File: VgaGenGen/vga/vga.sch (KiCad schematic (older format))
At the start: 22 parts, among them X25.175MHz CXO_DIP14

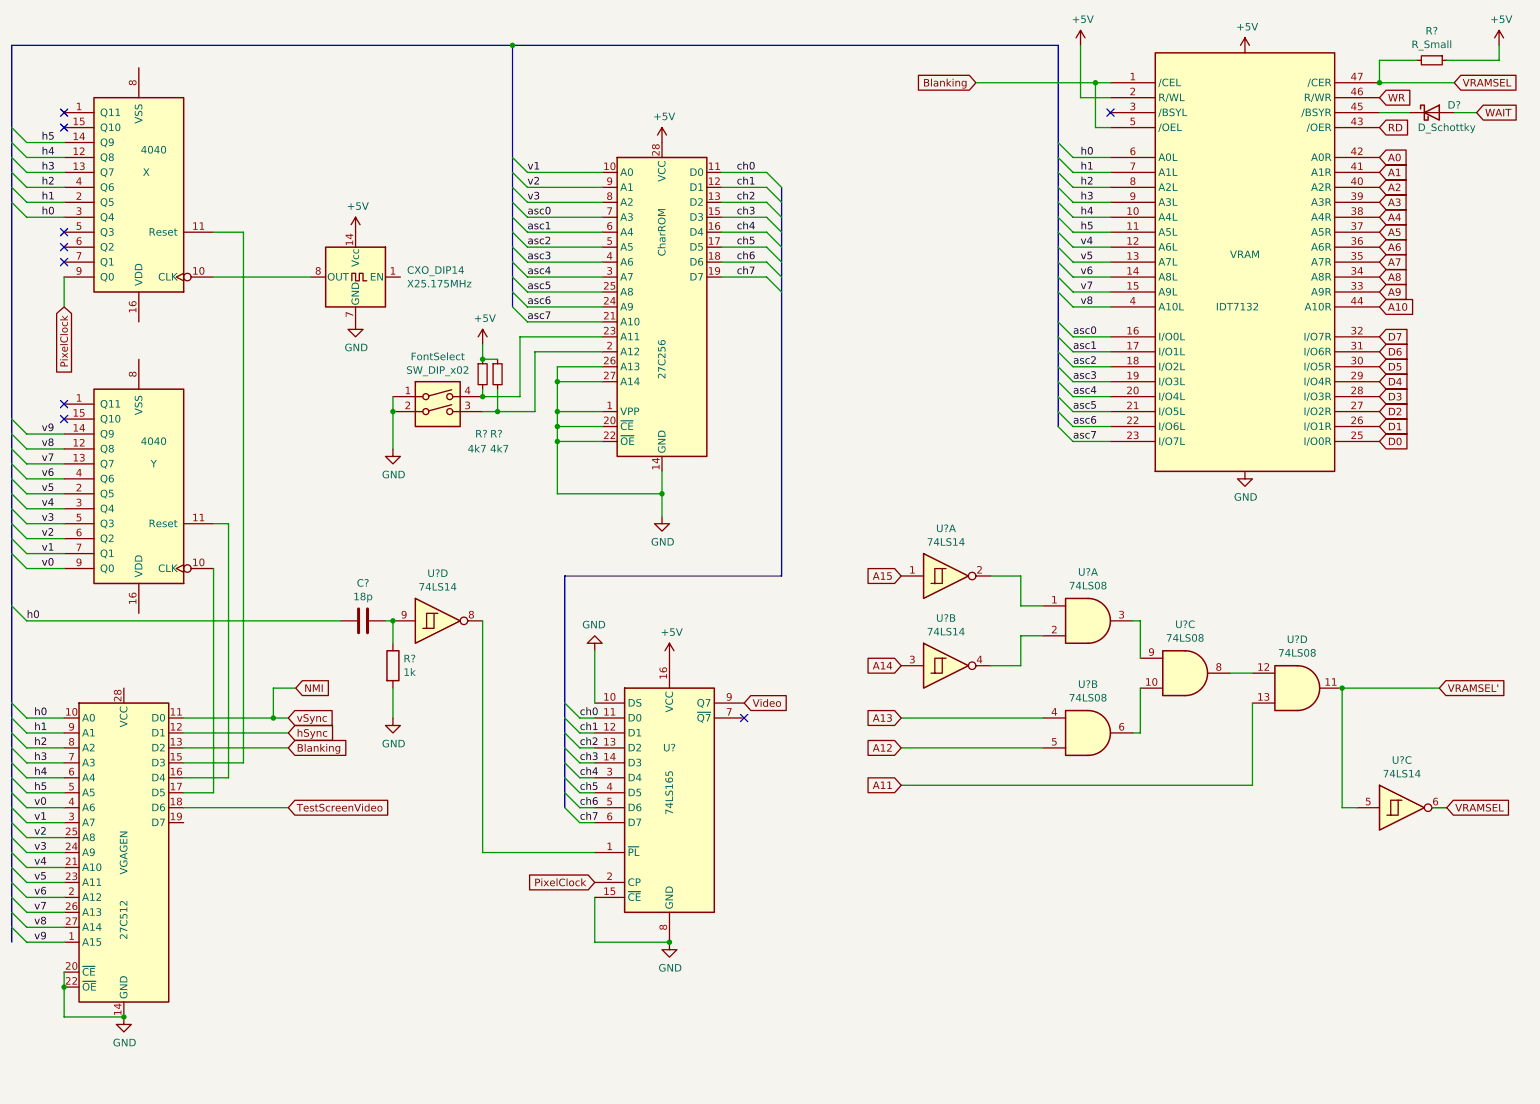
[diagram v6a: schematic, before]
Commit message: corrections to the VGA schematic, added vga.asm
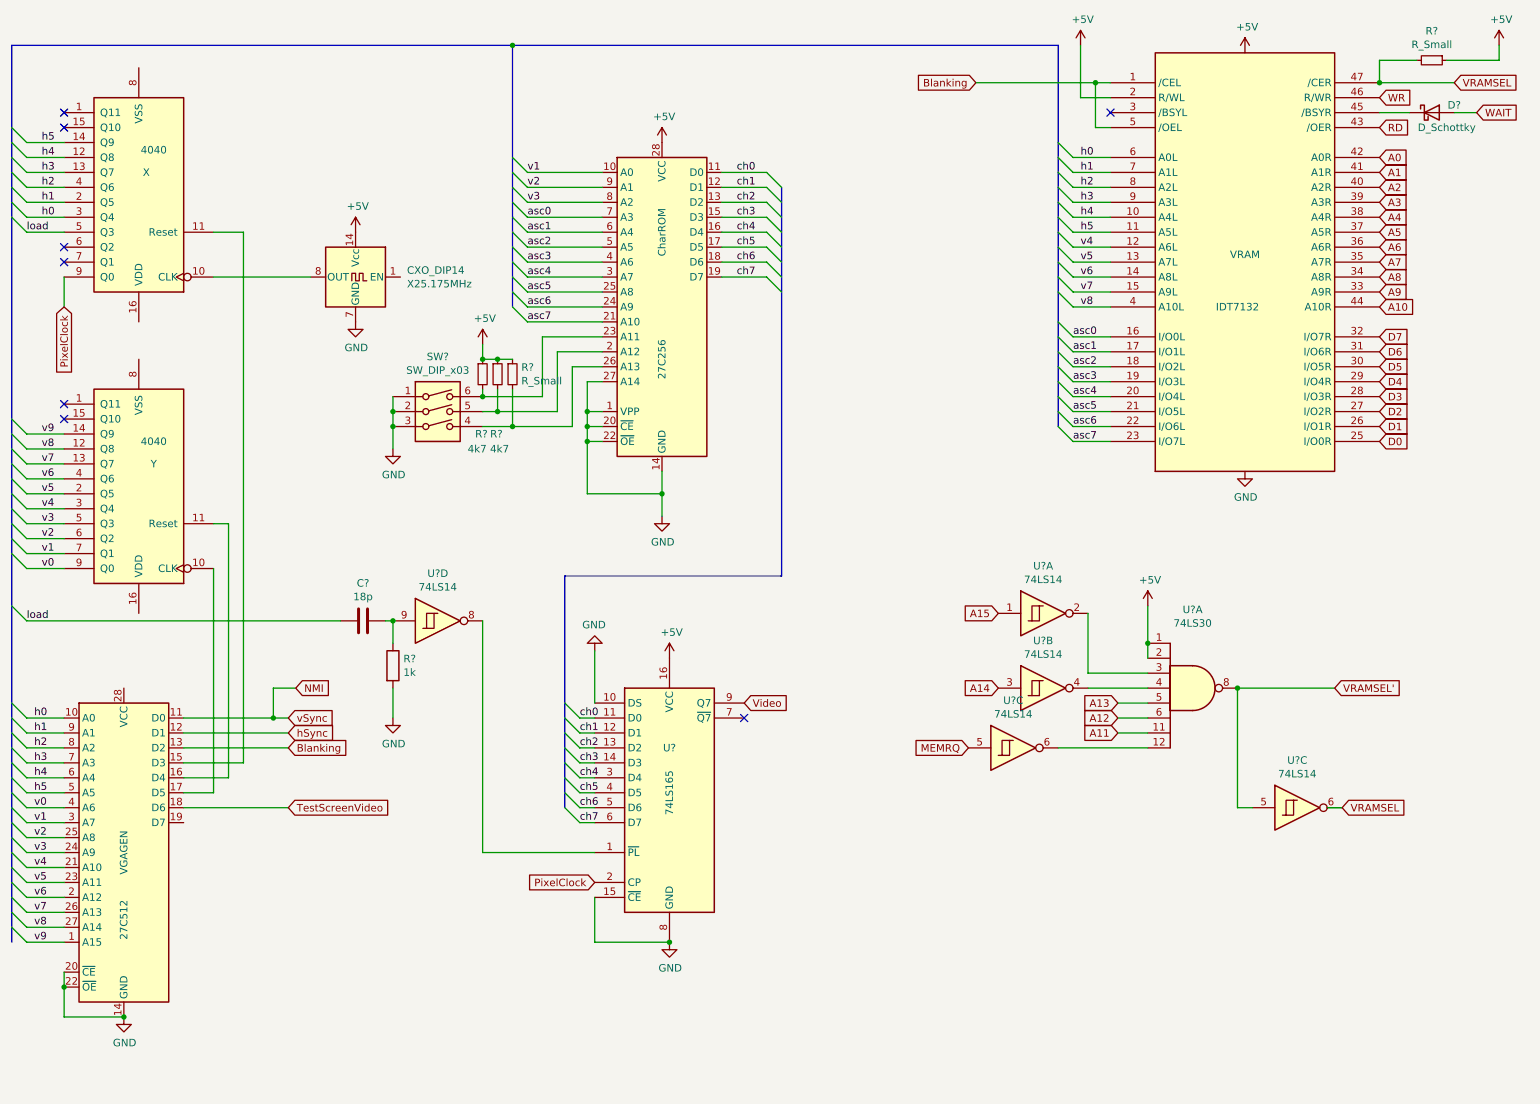
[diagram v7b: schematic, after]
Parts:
- removed FontSelect: SW_DIP_x02, symbol Switch:SW_DIP_x02
- removed U? (x4): 74LS08, symbol 74xx:74LS08
- added R?: R_Small, symbol Device:R_Small
- added SW?: SW_DIP_x03, symbol Switch:SW_DIP_x03
- added U?: 74LS30, symbol 74xx:74LS30
- added U?: 74LS14, symbol 74xx:74LS14
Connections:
- net +5V: now also R?.1, U?.1, U?.2
- net A11: now also U?.11
- net A12: now also U?.6
- net A13: now also U?.5
- net GND: now also SW?.1, SW?.2, SW?.3; no longer CharROM.26 (A13)
- net VRAMSEL': now also U?.8
- net h0: no longer C?.1
- net load: now reaches X.5 (Q3)
- net load: now also C?.1
- net at U?.2: now also U?.3
- net at U?.4: now also U?.4
- net at CharROM.2 (A12), R?.2: now also SW?.5
- net at CharROM.23 (A11), R?.2: now also SW?.6
- new net: CharROM.26 (A13), R?.2, SW?.4
- new net: U?.12, U?.6
- new net MEMRQ: U?.5
- no-connect marks 9 -> 8
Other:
- moved on the sheet: U?A, U?B, U?C
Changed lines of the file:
@@
 Entry Wire Line
 	950  4450 1050 4550
-Text Label 1050 4550 0    50   ~ 0
-h0
 Text GLabel 5850 5100 2    50   Input ~ 0
 Video
@@
 	1    0    0    -1
 $EndComp
-NoConn ~ 1300 1950
 NoConn ~ 1300 2050
 NoConn ~ 1300 2150
@@
 Wire Wire Line
 	8100 1050 8300 1050
-$Comp
-L Memory_EPROM:27C256 CharROM
-U 1 1 62173F7D
-P 5300 2450
-F 0 "CharROM" V 5300 2950 50  0000 C CNN
-F 1 "27C256" V 5300 2100 50  0000 C CNN
-F 2 "Package_DIP:DIP-28_W15.24mm" H 5300 2450 50  0001 C CNN
-F 3 "http://ww1.microchip.com/downloads/en/DeviceDoc/doc0014.pdf" H 5300 2450 50  0001 C CNN
-	1    5300 2450
-	1    0    0    -1
-$EndComp
 Entry Wire Line
 	6100 1650 6000 1550
@@
 	4900 2550 4400 2550
 Wire Wire Line
-	4600 3700 5300 3700
-Wire Wire Line
 	5300 3550 5300 3700
 Connection ~ 5300 3700
@@
 	5300 3700 5300 3850
 Wire Wire Line
-	4900 2850 4600 2850
-Wire Wire Line
-	4600 2850 4600 2950
-Wire Wire Line
-	4900 2950 4600 2950
-Connection ~ 4600 2950
-Wire Wire Line
-	4600 2950 4600 3150
-Wire Wire Line
-	4900 3150 4600 3150
-Connection ~ 4600 3150
-Wire Wire Line
-	4600 3150 4600 3250
-Wire Wire Line
-	4900 3250 4600 3250
-Connection ~ 4600 3250
-Wire Wire Line
-	4600 3250 4600 3350
-Wire Wire Line
-	4900 3350 4600 3350
-Connection ~ 4600 3350
-Wire Wire Line
-	4600 3350 4600 3700
+	4900 2950 4800 2950
 $Comp
 L power:+5V #PWR?
@@
 L 74xx:74LS14 U?
 U 1 1 6216906C
-P 7200 4250
-F 0 "U?" H 7200 4567 50  0000 C CNN
-F 1 "74LS14" H 7200 4476 50  0000 C CNN
-F 2 "" H 7200 4250 50  0001 C CNN
-F 3 "http://www.ti.com/lit/gpn/sn74LS14" H 7200 4250 50  0001 C CNN
-	1    7200 4250
+P 7850 4500
+F 0 "U?" H 7850 4817 50  0000 C CNN
+F 1 "74LS14" H 7850 4726 50  0000 C CNN
+F 2 "" H 7850 4500 50  0001 C CNN
+F 3 "http://www.ti.com/lit/gpn/sn74LS14" H 7850 4500 50  0001 C CNN
+	1    7850 4500
 	1    0    0    -1
 $EndComp
@@
 L 74xx:74LS14 U?
 U 2 1 62169072
-P 7200 4850
-F 0 "U?" H 7200 5167 50  0000 C CNN
-F 1 "74LS14" H 7200 5076 50  0000 C CNN
-F 2 "" H 7200 4850 50  0001 C CNN
-F 3 "http://www.ti.com/lit/gpn/sn74LS14" H 7200 4850 50  0001 C CNN
-	2    7200 4850
+P 7850 5000
+F 0 "U?" H 7850 5317 50  0000 C CNN
+F 1 "74LS14" H 7850 5226 50  0000 C CNN
+F 2 "" H 7850 5000 50  0001 C CNN
+F 3 "http://www.ti.com/lit/gpn/sn74LS14" H 7850 5000 50  0001 C CNN
+	2    7850 5000
 	1    0    0    -1
 $EndComp
@@
 L 74xx:74LS14 U?
 U 3 1 62169078
-P 10250 5800
-F 0 "U?" H 10250 6117 50  0000 C CNN
-F 1 "74LS14" H 10250 6026 50  0000 C CNN
-F 2 "" H 10250 5800 50  0001 C CNN
-F 3 "http://www.ti.com/lit/gpn/sn74LS14" H 10250 5800 50  0001 C CNN
-	3    10250 5800
-	1    0    0    -1
-$EndComp
-$Comp
-L 74xx:74LS08 U?
-U 1 1 6216907E
-P 8150 4550
-F 0 "U?" H 8150 4875 50  0000 C CNN
-F 1 "74LS08" H 8150 4784 50  0000 C CNN
-F 2 "" H 8150 4550 50  0001 C CNN
-F 3 "http://www.ti.com/lit/gpn/sn74LS08" H 8150 4550 50  0001 C CNN
-	1    8150 4550
-	1    0    0    -1
-$EndComp
-$Comp
-L 74xx:74LS08 U?
-U 2 1 62169084
-P 8150 5300
-F 0 "U?" H 8150 5625 50  0000 C CNN
-F 1 "74LS08" H 8150 5534 50  0000 C CNN
-F 2 "" H 8150 5300 50  0001 C CNN
-F 3 "http://www.ti.com/lit/gpn/sn74LS08" H 8150 5300 50  0001 C CNN
-	2    8150 5300
-	1    0    0    -1
-$EndComp
-$Comp
-L 74xx:74LS08 U?
-U 3 1 6216908A
-P 8800 4900
-F 0 "U?" H 8800 5225 50  0000 C CNN
-F 1 "74LS08" H 8800 5134 50  0000 C CNN
-F 2 "" H 8800 4900 50  0001 C CNN
-F 3 "http://www.ti.com/lit/gpn/sn74LS08" H 8800 4900 50  0001 C CNN
-	3    8800 4900
-	1    0    0    -1
-$EndComp
-$Comp
-L 74xx:74LS08 U?
-U 4 1 62169090
-P 9550 5000
-F 0 "U?" H 9550 5325 50  0000 C CNN
-F 1 "74LS08" H 9550 5234 50  0000 C CNN
-F 2 "" H 9550 5000 50  0001 C CNN
-F 3 "http://www.ti.com/lit/gpn/sn74LS08" H 9550 5000 50  0001 C CNN
-	4    9550 5000
-	1    0    0    -1
-$EndComp
-Wire Wire Line
-	8500 4800 8500 4550
-Wire Wire Line
-	8500 4550 8450 4550
-Wire Wire Line
-	8500 5000 8500 5300
-Wire Wire Line
-	8500 5300 8450 5300
-Wire Wire Line
-	7850 4450 7700 4450
-Wire Wire Line
-	7700 4450 7700 4250
-Wire Wire Line
-	7700 4250 7500 4250
-Wire Wire Line
-	7500 4850 7700 4850
-Wire Wire Line
-	7700 4850 7700 4650
-Wire Wire Line
-	7700 4650 7850 4650
-Wire Wire Line
-	9850 5000 9850 5800
-Wire Wire Line
-	9850 5800 9950 5800
-Wire Wire Line
-	9100 4900 9250 4900
-Text GLabel 10550 5800 2    50   Input ~ 0
+P 9550 5800
+F 0 "U?" H 9550 6117 50  0000 C CNN
+F 1 "74LS14" H 9550 6026 50  0000 C CNN
+F 2 "" H 9550 5800 50  0001 C CNN
+F 3 "http://www.ti.com/lit/gpn/sn74LS14" H 9550 5800 50  0001 C CNN
+	3    9550 5800
+	1    0    0    -1
+$EndComp
+Wire Wire Line
+	9150 5000 9150 5800
+Wire Wire Line
+	9150 5800 9250 5800
+Text GLabel 9850 5800 2    50   Input ~ 0
 VRAMSEL
-Text GLabel 10500 5000 2    50   Input ~ 0
+Text GLabel 9800 5000 2    50   Input ~ 0
 VRAMSEL'
-Connection ~ 9850 5000
-Text GLabel 6900 4850 0    50   Input ~ 0
+Text GLabel 7550 5000 0    50   Input ~ 0
 A14
-Text GLabel 6900 4250 0    50   Input ~ 0
+Text GLabel 7550 4500 0    50   Input ~ 0
 A15
-Text GLabel 6900 5200 0    50   Input ~ 0
+Text GLabel 8350 5100 0    50   Input ~ 0
 A13
-Text GLabel 6900 5400 0    50   Input ~ 0
+Text GLabel 8350 5200 0    50   Input ~ 0
 A12
-Text GLabel 6900 5650 0    50   Input ~ 0
+Text GLabel 8350 5300 0    50   Input ~ 0
 A11
 Wire Wire Line
-	6900 5200 7850 5200
-Wire Wire Line
-	7850 5400 6900 5400
-Wire Wire Line
-	6900 5650 9250 5650
-Wire Wire Line
-	9250 5100 9250 5650
-Wire Wire Line
-	10450 5800 10550 5800
-Wire Wire Line
-	10500 5000 9850 5000
+	9750 5800 9850 5800
+Wire Wire Line
+	9800 5000 9150 5000
 Wire Bus Line
 	950  700  4300 700
@@
 Wire Bus Line
 	4300 700  7950 700
-$Comp
-L Switch:SW_DIP_x02 FontSelect
-U 1 1 621A6CFD
-P 3800 3150
-F 0 "FontSelect" H 3800 3517 50  0000 C CNN
-F 1 "SW_DIP_x02" H 3800 3426 50  0000 C CNN
-F 2 "" H 3800 3150 50  0001 C CNN
-F 3 "~" H 3800 3150 50  0001 C CNN
-	1    3800 3150
-	1    0    0    -1
-$EndComp
 $Comp
 L power:GND #PWR?
@@
 $EndComp
 Wire Wire Line
-	3500 3400 3500 3150
-Connection ~ 3500 3150
-Wire Wire Line
-	3500 3150 3500 3050
-Wire Wire Line
-	4900 2750 4450 2750
-Wire Wire Line
-	4450 2750 4450 3150
-Wire Wire Line
-	4450 3150 4200 3150
-Wire Wire Line
-	4900 2650 4350 2650
-Wire Wire Line
-	4350 2650 4350 3050
-Wire Wire Line
-	4350 3050 4100 3050
+	4900 2750 4600 2750
+Wire Wire Line
+	4900 2650 4500 2650
 $Comp
 L Device:R_Small R?
@@
 Wire Wire Line
 	4100 3000 4100 3050
-Connection ~ 4100 3050
 Wire Wire Line
 	4200 2800 4100 2800
@@
 Wire Wire Line
 	10900 800  10900 700
+$Comp
+L 74xx:74LS30 U?
+U 1 1 623C44D8
+P 8850 5000
+F 0 "U?" H 8850 5525 50  0000 C CNN
+F 1 "74LS30" H 8850 5434 50  0000 C CNN
+F 2 "" H 8850 5000 50  0001 C CNN
+F 3 "http://www.ti.com/lit/gpn/sn74LS30" H 8850 5000 50  0001 C CNN
+	1    8850 5000
+	1    0    0    -1
+$EndComp
+Wire Wire Line
+	8350 5100 8550 5100
+Wire Wire Line
+	8350 5200 8550 5200
+Wire Wire Line
+	8350 5300 8550 5300
+Wire Wire Line
+	8550 5000 8150 5000
+Wire Wire Line
+	8550 4900 8150 4900
+Wire Wire Line
+	8150 4900 8150 4500
+$Comp
+L power:+5V #PWR?
+U 1 1 62458EBA
+P 8550 4450
+F 0 "#PWR?" H 8550 4300 50  0001 C CNN
+F 1 "+5V" H 8565 4623 50  0000 C CNN
+F 2 "" H 8550 4450 50  0001 C CNN
+F 3 "" H 8550 4450 50  0001 C CNN
+	1    8550 4450
+	1    0    0    -1
+$EndComp
+Wire Wire Line
+	8550 4450 8550 4700
+Connection ~ 8550 4700
+Wire Wire Line
+	8550 4700 8550 4800
+Connection ~ 9150 5000
+Text GLabel 7350 5400 0    50   Input ~ 0
+MEMRQ
+$Comp
+L Switch:SW_DIP_x03 SW?
+U 1 1 623E144D
+P 3800 3250
+F 0 "SW?" H 3800 3717 50  0000 C CNN
+F 1 "SW_DIP_x03" H 3800 3626 50  0000 C CNN
+F 2 "" H 3800 3250 50  0001 C CNN
+F 3 "~" H 3800 3250 50  0001 C CNN
+	1    3800 3250
+	1    0    0    -1
+$EndComp
+Wire Wire Line
+	3500 3250 3500 3400
+Connection ~ 4100 3050
+Wire Wire Line
+	3500 3050 3500 3150
+Connection ~ 3500 3250
+Connection ~ 3500 3150
+Wire Wire Line
+	3500 3150 3500 3250
+Wire Wire Line
+	4800 2950 4800 3150
+Wire Wire Line
+	4800 3700 5300 3700
+$Comp
+L Memory_EPROM:27C256 CharROM
+U 1 1 62173F7D
+P 5300 2450
+F 0 "CharROM" V 5300 2950 50  0000 C CNN
+F 1 "27C256" V 5300 2100 50  0000 C CNN
+F 2 "Package_DIP:DIP-28_W15.24mm" H 5300 2450 50  0001 C CNN
+F 3 "http://ww1.microchip.com/downloads/en/DeviceDoc/doc0014.pdf" H 5300 2450 50  0001 C CNN
+	1    5300 2450
+	1    0    0    -1
+$EndComp
+Wire Wire Line
+	4900 3150 4800 3150
+Connection ~ 4800 3150
+Wire Wire Line
+	4800 3150 4800 3250
+Wire Wire Line
+	4900 3250 4800 3250
+Connection ~ 4800 3250
+Wire Wire Line
+	4800 3250 4800 3350
+Wire Wire Line
+	4900 3350 4800 3350
+Connection ~ 4800 3350
+Wire Wire Line
+	4800 3350 4800 3700
+Entry Wire Line
+	950  1850 1050 1950
+Wire Wire Line
+	1300 1950 1050 1950
+Text Label 1050 1950 0    50   ~ 0
+load
+Text Label 1050 4550 0    50   ~ 0
+load
+$Comp
+L 74xx:74LS14 U?
+U 3 1 6243E887
+P 7650 5400
+F 0 "U?" H 7650 5717 50  0000 C CNN
+F 1 "74LS14" H 7650 5626 50  0000 C CNN
+F 2 "" H 7650 5400 50  0001 C CNN
+F 3 "http://www.ti.com/lit/gpn/sn74LS14" H 7650 5400 50  0001 C CNN
+	3    7650 5400
+	1    0    0    -1
+$EndComp
+Wire Wire Line
+	7950 5400 8550 5400
+Wire Wire Line
+	4700 2850 4700 3250
+Wire Wire Line
+	4700 2850 4900 2850
+Wire Wire Line
+	4100 3250 4300 3250
+Wire Wire Line
+	4600 3150 4600 2750
+Wire Wire Line
+	4200 3150 4600 3150
+Wire Wire Line
+	4500 3050 4500 2650
+Wire Wire Line
+	4100 3050 4500 3050
+$Comp
+L Device:R_Small R?
+U 1 1 62465F54
+P 4300 2900
+F 0 "R?" H 4359 2946 50  0000 L CNN
+F 1 "R_Small" H 4359 2855 50  0000 L CNN
+F 2 "" H 4300 2900 50  0001 C CNN
+F 3 "~" H 4300 2900 50  0001 C CNN
+	1    4300 2900
+	1    0    0    -1
+$EndComp
+Wire Wire Line
+	4300 2800 4200 2800
+Connection ~ 4200 2800
+Wire Wire Line
+	4300 3000 4300 3250
 Wire Bus Line
 	6100 1650 6100 4250
@@
 Wire Bus Line
 	950  700  950  6700
+Connection ~ 4300 3250
+Wire Wire Line
+	4300 3250 4700 3250
 $EndSCHEMATC

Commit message: moved dev drivers and utils to separate folders
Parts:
- added C?: 1u, symbol Device:C_Small
- added D?: D_Schottky, symbol Device:D_Schottky
- added R?: 1k, symbol Device:R_Small
- added R?: 330k, symbol Device:R_Small
- added U?: 74LS14, symbol 74xx:74LS14
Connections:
- net GND: now also C?.2
- net asc7: now also D?.2 (A), R?.2; no longer VRAM.23 (I/O7L)
- new net: R?.1, VRAM.23 (I/O7L)
- new net: D?.1 (K), R?.1, U?.12
- new net: C?.1, R?.2, U?.13
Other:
- moved on the sheet: U?C
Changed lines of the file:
@@
 	7950 3250 8050 3350
-Wire Wire Line
-	8300 3350 8050 3350
 Wire Wire Line
 	8300 3250 8050 3250
@@
 	8550 4700 8550 4800
 Connection ~ 9150 5000
-Text GLabel 7350 5400 0    50   Input ~ 0
+Text GLabel 7550 5650 0    50   Input ~ 0
 MEMRQ
 $Comp
@@
 L 74xx:74LS14 U?
 U 3 1 6243E887
-P 7650 5400
-F 0 "U?" H 7650 5717 50  0000 C CNN
-F 1 "74LS14" H 7650 5626 50  0000 C CNN
-F 2 "" H 7650 5400 50  0001 C CNN
-F 3 "http://www.ti.com/lit/gpn/sn74LS14" H 7650 5400 50  0001 C CNN
-	3    7650 5400
-	1    0    0    -1
-$EndComp
-Wire Wire Line
-	7950 5400 8550 5400
+P 7850 5650
+F 0 "U?" H 7850 5967 50  0000 C CNN
+F 1 "74LS14" H 7850 5876 50  0000 C CNN
+F 2 "" H 7850 5650 50  0001 C CNN
+F 3 "http://www.ti.com/lit/gpn/sn74LS14" H 7850 5650 50  0001 C CNN
+	3    7850 5650
+	1    0    0    -1
+$EndComp
 Wire Wire Line
 	4700 2850 4700 3250
@@
 Wire Wire Line
 	4300 3000 4300 3250
+Connection ~ 4300 3250
+Wire Wire Line
+	4300 3250 4700 3250
+Wire Wire Line
+	8150 5650 8150 5400
+Wire Wire Line
+	8150 5400 8550 5400
+$Comp
+L Device:R_Small R?
+U 1 1 627DE5FC
+P 8200 3650
+F 0 "R?" V 8300 3650 50  0000 C CNN
+F 1 "1k" V 8095 3650 50  0000 C CNN
+F 2 "" H 8200 3650 50  0001 C CNN
+F 3 "~" H 8200 3650 50  0001 C CNN
+	1    8200 3650
+	0    1    1    0
+$EndComp
+Wire Wire Line
+	8300 3650 8300 3350
+Wire Wire Line
+	8100 3650 8100 3350
+Wire Wire Line
+	8100 3350 8050 3350
+$Comp
+L 74xx:74LS14 U?
+U 6 1 627F2FB8
+P 7250 3650
+F 0 "U?" H 7250 3967 50  0000 C CNN
+F 1 "74LS14" H 7250 3876 50  0000 C CNN
+F 2 "" H 7250 3650 50  0001 C CNN
+F 3 "http://www.ti.com/lit/gpn/sn74LS14" H 7250 3650 50  0001 C CNN
+	6    7250 3650
+	1    0    0    -1
+$EndComp
+$Comp
+L Device:D_Schottky D?
+U 1 1 627F48A8
+P 7800 3650
+F 0 "D?" H 7800 3867 50  0000 C CNN
+F 1 "D_Schottky" H 7800 3776 50  0000 C CNN
+F 2 "" H 7800 3650 50  0001 C CNN
+F 3 "~" H 7800 3650 50  0001 C CNN
+	1    7800 3650
+	1    0    0    -1
+$EndComp
+Wire Wire Line
+	7650 3650 7600 3650
+Wire Wire Line
+	7950 3650 8100 3650
+Connection ~ 8100 3650
+$Comp
+L Device:R_Small R?
+U 1 1 62808D1B
+P 7200 3150
+F 0 "R?" V 7004 3150 50  0000 C CNN
+F 1 "330k" V 7095 3150 50  0000 C CNN
+F 2 "" H 7200 3150 50  0001 C CNN
+F 3 "~" H 7200 3150 50  0001 C CNN
+	1    7200 3150
+	0    1    1    0
+$EndComp
+Wire Wire Line
+	7600 3650 7600 3150
+Wire Wire Line
+	7600 3150 7300 3150
+Connection ~ 7600 3650
+Wire Wire Line
+	7600 3650 7550 3650
+Wire Wire Line
+	7100 3150 6950 3150
+Wire Wire Line
+	6950 3150 6950 3650
+$Comp
+L Device:C_Small C?
+U 1 1 6281E9AB
+P 6950 4000
+F 0 "C?" H 7042 4046 50  0000 L CNN
+F 1 "1u" H 7042 3955 50  0000 L CNN
+F 2 "" H 6950 4000 50  0001 C CNN
+F 3 "~" H 6950 4000 50  0001 C CNN
+	1    6950 4000
+	1    0    0    -1
+$EndComp
+Wire Wire Line
+	6950 3900 6950 3650
 Wire Bus Line
 	6100 1650 6100 4250
@@
 Wire Bus Line
 	950  700  950  6700
-Connection ~ 4300 3250
-Wire Wire Line
-	4300 3250 4700 3250
+Connection ~ 6950 3650
+$Comp
+L power:GND #PWR?
+U 1 1 62829BE7
+P 6950 4100
+F 0 "#PWR?" H 6950 3850 50  0001 C CNN
+F 1 "GND" H 6955 3927 50  0000 C CNN
+F 2 "" H 6950 4100 50  0001 C CNN
+F 3 "" H 6950 4100 50  0001 C CNN
+	1    6950 4100
+	1    0    0    -1
+$EndComp
 $EndSCHEMATC
